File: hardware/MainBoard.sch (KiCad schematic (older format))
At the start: 33 parts, among them P1 CONN_01X07, P2 CONN_01X04, P3 CONN_01X04, P4 CONN_01X07, P5 ON/OFF, P6 BATTERY

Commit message: Fix schematic libraries
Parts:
- P?: symbol USB_OTG -> USB_OTG-RESCUE-MainBoard
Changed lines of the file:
@@
 EESchema Schematic File Version 2
+LIBS:MainBoard-rescue
 LIBS:power
 LIBS:device
@@
 LIBS:contrib
 LIBS:valves
-LIBS:ATSAMD21G18A-AU
-LIBS:MCP73831T-2ACI_OT
-LIBS:theinventorhouse
-LIBS:B3U-1000P
 LIBS:MainBoard-cache
 EELAYER 25 0
@@
 $Bitmap
 Pos 9695 7065
-Scale 1,000000
+Scale 1.000000
 Data
 89 50 4E 47 0D 0A 1A 0A 00 00 00 0D 49 48 44 52 00 00 01 77 00 00 01 29 08 06 00 00 00 68 44 62
@@
 POWER, CHARGER & FILTERING
 $Comp
-L USB_OTG P?
+L USB_OTG-RESCUE-MainBoard P?
 U 1 1 5AD40F68
 P 8980 975

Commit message: check button
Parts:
- removed S?: B3U-1000P, SW_B3U-1000P, symbol B3U-1000P
- added R?: 10k, symbol R_Small
- added SW?: SW_Push, symbol SW_Push
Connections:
- net +3V3: now also R?.2
- net GND: now also SW?.1
- net RESET: now also R?.1, SW?.2
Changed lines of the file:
@@
 EESchema Schematic File Version 2
-LIBS:MainBoard-rescue
 LIBS:power
 LIBS:device
@@
 LIBS:contrib
 LIBS:valves
+LIBS:CatSatZero
+LIBS:74xgxx
+LIBS:ac-dc
+LIBS:actel
+LIBS:allegro
+LIBS:Altera
+LIBS:analog_devices
+LIBS:battery_management
+LIBS:bbd
+LIBS:bosch
+LIBS:brooktre
+LIBS:cmos_ieee
+LIBS:dc-dc
+LIBS:diode
+LIBS:elec-unifil
+LIBS:ESD_Protection
+LIBS:ftdi
+LIBS:gennum
+LIBS:graphic_symbols
+LIBS:hc11
+LIBS:infineon
+LIBS:intersil
+LIBS:ir
+LIBS:Lattice
+LIBS:leds
+LIBS:LEM
+LIBS:logic_programmable
+LIBS:maxim
+LIBS:mechanical
+LIBS:microchip_dspic33dsc
+LIBS:microchip_pic10mcu
+LIBS:microchip_pic12mcu
+LIBS:microchip_pic16mcu
+LIBS:microchip_pic18mcu
+LIBS:microchip_pic24mcu
+LIBS:microchip_pic32mcu
+LIBS:modules
+LIBS:motor_drivers
+LIBS:motors
+LIBS:msp430
+LIBS:nordicsemi
+LIBS:nxp_armmcu
+LIBS:nxp
+LIBS:onsemi
+LIBS:Oscillators
+LIBS:Power_Management
+LIBS:powerint
+LIBS:pspice
+LIBS:references
+LIBS:relays
+LIBS:rfcom
+LIBS:RFSolutions
+LIBS:sensors
+LIBS:silabs
+LIBS:stm8
+LIBS:stm32
+LIBS:supertex
+LIBS:switches
+LIBS:transf
+LIBS:triac_thyristor
+LIBS:ttl_ieee
+LIBS:video
+LIBS:wiznet
+LIBS:Worldsemi
+LIBS:Xicor
+LIBS:zetex
+LIBS:Zilog
 LIBS:MainBoard-cache
 EELAYER 25 0
@@
 	1    0    0    -1
 $EndComp
-$Comp
-L B3U-1000P S?
-U 1 1 5AD4D846
-P 6510 4980
-F 0 "S?" H 6209 5181 50  0000 L BNN
-F 1 "B3U-1000P" H 6209 4679 50  0000 L BNN
-F 2 "SW_B3U-1000P" H 6510 4980 50  0001 L BNN
-F 3 "None" H 6510 4980 50  0001 L BNN
-F 4 "Omron" H 6510 4980 50  0001 L BNN "Campo4"
-F 5 "B3U-1000P" H 6510 4980 50  0001 L BNN "Campo5"
-F 6 "Switch Tactile N.O. SPST Round Button Gull Wing 0.05A 12VDC 1.5N SMD Embossed T/R" H 6510 4980 50  0001 L BNN "Campo6"
-F 7 "0.69 USD" H 6510 4980 50  0001 L BNN "Campo7"
-F 8 "Good" H 6510 4980 50  0001 L BNN "Campo8"
-	1    6510 4980
-	1    0    0    -1
-$EndComp
-Text Label 7155 4980 0    60   ~ 0
+Text Label 6655 5145 0    60   ~ 0
 RESET
 $Comp
 L GND #PWR?
 U 1 1 5AD4E61D
-P 5875 5030
-F 0 "#PWR?" H 5875 4780 50  0001 C CNN
-F 1 "GND" H 5875 4880 50  0000 C CNN
-F 2 "" H 5875 5030 50  0000 C CNN
-F 3 "" H 5875 5030 50  0000 C CNN
-	1    5875 5030
+P 5725 5195
+F 0 "#PWR?" H 5725 4945 50  0001 C CNN
+F 1 "GND" H 5725 5045 50  0000 C CNN
+F 2 "" H 5725 5195 50  0000 C CNN
+F 3 "" H 5725 5195 50  0000 C CNN
+	1    5725 5195
 	1    0    0    -1
 $EndComp
@@
 	3555 2405 3700 2405
 Wire Wire Line
-	3700 2405 3700 1925
+	3700 2405 3700 2305
+Wire Wire Line
+	3700 2305 3700 2205
+Wire Wire Line
+	3700 2205 3700 2105
+Wire Wire Line
+	3700 2105 3700 1925
 Wire Wire Line
 	3555 2305 3700 2305
@@
 	3555 4805 3605 4805
 Wire Wire Line
-	3605 4805 3605 5185
+	3605 4805 3605 4905
+Wire Wire Line
+	3605 4905 3605 5005
+Wire Wire Line
+	3605 5005 3605 5105
+Wire Wire Line
+	3605 5105 3605 5185
 Wire Wire Line
 	3555 5105 3605 5105
@@
 	11205 3355 11205 3365
 Wire Wire Line
-	8650 2595 9520 2595
+	8650 2595 8895 2595
+Wire Wire Line
+	8895 2595 9110 2595
+Wire Wire Line
+	9110 2595 9520 2595
 Wire Wire Line
 	8895 2595 8895 2465
@@
 Connection ~ 8895 2595
 Wire Wire Line
-	10470 2595 10985 2595
+	10470 2595 10520 2595
+Wire Wire Line
+	10520 2595 10710 2595
+Wire Wire Line
+	10710 2595 10885 2595
+Wire Wire Line
+	10885 2595 10985 2595
 Wire Wire Line
 	10885 2595 10885 2640
@@
 	10520 2840 10520 2945
 Wire Wire Line
-	10710 2840 10710 3005
+	10710 2840 10710 2945
+Wire Wire Line
+	10710 2945 10710 3005
 Wire Wire Line
 	10885 2945 10885 2840
 Wire Wire Line
-	10520 2945 10885 2945
+	10520 2945 10710 2945
+Wire Wire Line
+	10710 2945 10885 2945
 Connection ~ 10710 2945
 Wire Notes Line
@@
 	5275 6540 6965 6540
 Wire Wire Line
-	5450 2500 5450 2585
+	5450 2500 5450 2540
+Wire Wire Line
+	5450 2540 5450 2585
 Wire Wire Line
 	5450 2785 5450 2845
@@
 	6060 2225 6060 2080
 Wire Wire Line
-	6010 4980 5875 4980
-Wire Wire Line
-	5875 4980 5875 5030
-Wire Wire Line
-	7010 4980 7155 4980
+	5860 5145 5725 5145
+Wire Wire Line
+	5725 5145 5725 5195
+Wire Wire Line
+	6260 5145 6505 5145
+Wire Wire Line
+	6505 5145 6655 5145
 Wire Wire Line
 	2155 3905 1990 3905
@@
 	8135 4285 8135 4315
 Wire Wire Line
-	1435 1940 1435 2405
-Wire Wire Line
-	1235 1940 1235 2505
+	1435 1940 1435 2100
+Wire Wire Line
+	1435 2100 1435 2405
+Wire Wire Line
+	1235 1940 1235 2100
+Wire Wire Line
+	1235 2100 1235 2505
 Connection ~ 1435 2100
 Connection ~ 1235 2100
@@
 	1345 1550 1345 1630
 Wire Wire Line
-	1235 1630 1435 1630
+	1235 1630 1345 1630
+Wire Wire Line
+	1345 1630 1435 1630
 Connection ~ 1345 1630
 Wire Wire Line
@@
 	1    0    0    -1
 $EndComp
+$Comp
+L +3.3V #PWR?
+U 1 1 5AD55919
+P 6505 4730
+F 0 "#PWR?" H 6505 4580 50  0001 C CNN
+F 1 "+3.3V" H 6505 4870 50  0000 C CNN
+F 2 "" H 6505 4730 50  0000 C CNN
+F 3 "" H 6505 4730 50  0000 C CNN
+	1    6505 4730
+	1    0    0    -1
+$EndComp
+$Comp
+L R_Small R?
+U 1 1 5AD55C99
+P 6505 4905
+F 0 "R?" H 6535 4925 50  0000 L CNN
+F 1 "10k" H 6535 4865 50  0000 L CNN
+F 2 "" H 6505 4905 50  0000 C CNN
+F 3 "" H 6505 4905 50  0000 C CNN
+	1    6505 4905
+	-1   0    0    1
+$EndComp
+Wire Wire Line
+	6505 4730 6505 4805
+Wire Wire Line
+	6505 5005 6505 5145
+Connection ~ 6505 5145
+$Comp
+L SW_Push SW?
+U 1 1 5AD574E0
+P 6060 5145
+F 0 "SW?" H 6110 5245 50  0000 L CNN
+F 1 "SW_Push" H 6060 5085 50  0000 C CNN
+F 2 "" H 6060 5345 50  0001 C CNN
+F 3 "" H 6060 5345 50  0001 C CNN
+	1    6060 5145
+	1    0    0    -1
+$EndComp

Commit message: Shottcky diode fix
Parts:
- removed D?: MBR120, symbol D_Schottky
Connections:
- net VCC: now also C?.1, D?.1 (K), U?.3 (IN)
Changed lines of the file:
@@
-$EndComp
-$Comp
-L D_Schottky D?
-U 1 1 5AD43E7A
-P 8650 2315
-F 0 "D?" H 8650 2415 50  0000 C CNN
-F 1 "MBR120" H 8645 2245 50  0000 C CNN
-F 2 "" H 8650 2315 50  0000 C CNN
-F 3 "" H 8650 2315 50  0000 C CNN
-	1    8650 2315
-	0    -1   -1   0
 $EndComp
 $Comp
@@
 	2155 2605 1970 2605
 Wire Wire Line
-	3555 2405 3700 2405
-Wire Wire Line
-	3700 2405 3700 2305
-Wire Wire Line
-	3700 2305 3700 2205
-Wire Wire Line
-	3700 2205 3700 2105
-Wire Wire Line
-	3700 2105 3700 1925
+	3700 2405 3555 2405
+Wire Wire Line
+	3700 1925 3700 2405
 Wire Wire Line
 	3555 2305 3700 2305
@@
 	3555 4805 3605 4805
 Wire Wire Line
-	3605 4805 3605 4905
-Wire Wire Line
-	3605 4905 3605 5005
-Wire Wire Line
-	3605 5005 3605 5105
-Wire Wire Line
-	3605 5105 3605 5185
+	3605 4805 3605 5185
 Wire Wire Line
 	3555 5105 3605 5105
@@
 	11205 3355 11205 3365
 Wire Wire Line
-	8650 2595 8895 2595
-Wire Wire Line
-	8895 2595 9110 2595
-Wire Wire Line
-	9110 2595 9520 2595
+	8650 2595 9520 2595
 Wire Wire Line
 	8895 2595 8895 2465
@@
 	8895 2165 8895 2085
 Wire Wire Line
-	8650 2595 8650 2465
+	8650 2100 8650 2595
 Connection ~ 8895 2595
 Wire Wire Line
-	10470 2595 10520 2595
-Wire Wire Line
-	10520 2595 10710 2595
-Wire Wire Line
-	10710 2595 10885 2595
-Wire Wire Line
-	10885 2595 10985 2595
+	10470 2595 10985 2595
 Wire Wire Line
 	10885 2595 10885 2640
@@
 	10520 2840 10520 2945
 Wire Wire Line
-	10710 2840 10710 2945
-Wire Wire Line
-	10710 2945 10710 3005
+	10710 2840 10710 3005
 Wire Wire Line
 	10885 2945 10885 2840
 Wire Wire Line
-	10520 2945 10710 2945
-Wire Wire Line
-	10710 2945 10885 2945
+	10520 2945 10885 2945
 Connection ~ 10710 2945
 Wire Notes Line
@@
 	8290 2225 8290 2130
 Wire Wire Line
-	8650 2165 8650 2100
-Wire Wire Line
 	8330 680  8330 775
 Wire Wire Line
@@
 	5275 6540 6965 6540
 Wire Wire Line
-	5450 2500 5450 2540
-Wire Wire Line
-	5450 2540 5450 2585
+	5450 2500 5450 2585
 Wire Wire Line
 	5450 2785 5450 2845
@@
 	5725 5145 5725 5195
 Wire Wire Line
-	6260 5145 6505 5145
-Wire Wire Line
-	6505 5145 6655 5145
+	6260 5145 6655 5145
 Wire Wire Line
 	2155 3905 1990 3905
@@
 	8135 4285 8135 4315
 Wire Wire Line
-	1435 1940 1435 2100
-Wire Wire Line
-	1435 2100 1435 2405
-Wire Wire Line
-	1235 1940 1235 2100
-Wire Wire Line
-	1235 2100 1235 2505
+	1435 1940 1435 2405
+Wire Wire Line
+	1235 1940 1235 2505
 Connection ~ 1435 2100
 Connection ~ 1235 2100
@@
 	1345 1550 1345 1630
 Wire Wire Line
-	1235 1630 1345 1630
-Wire Wire Line
-	1345 1630 1435 1630
+	1235 1630 1435 1630
 Connection ~ 1345 1630
 Wire Wire Line

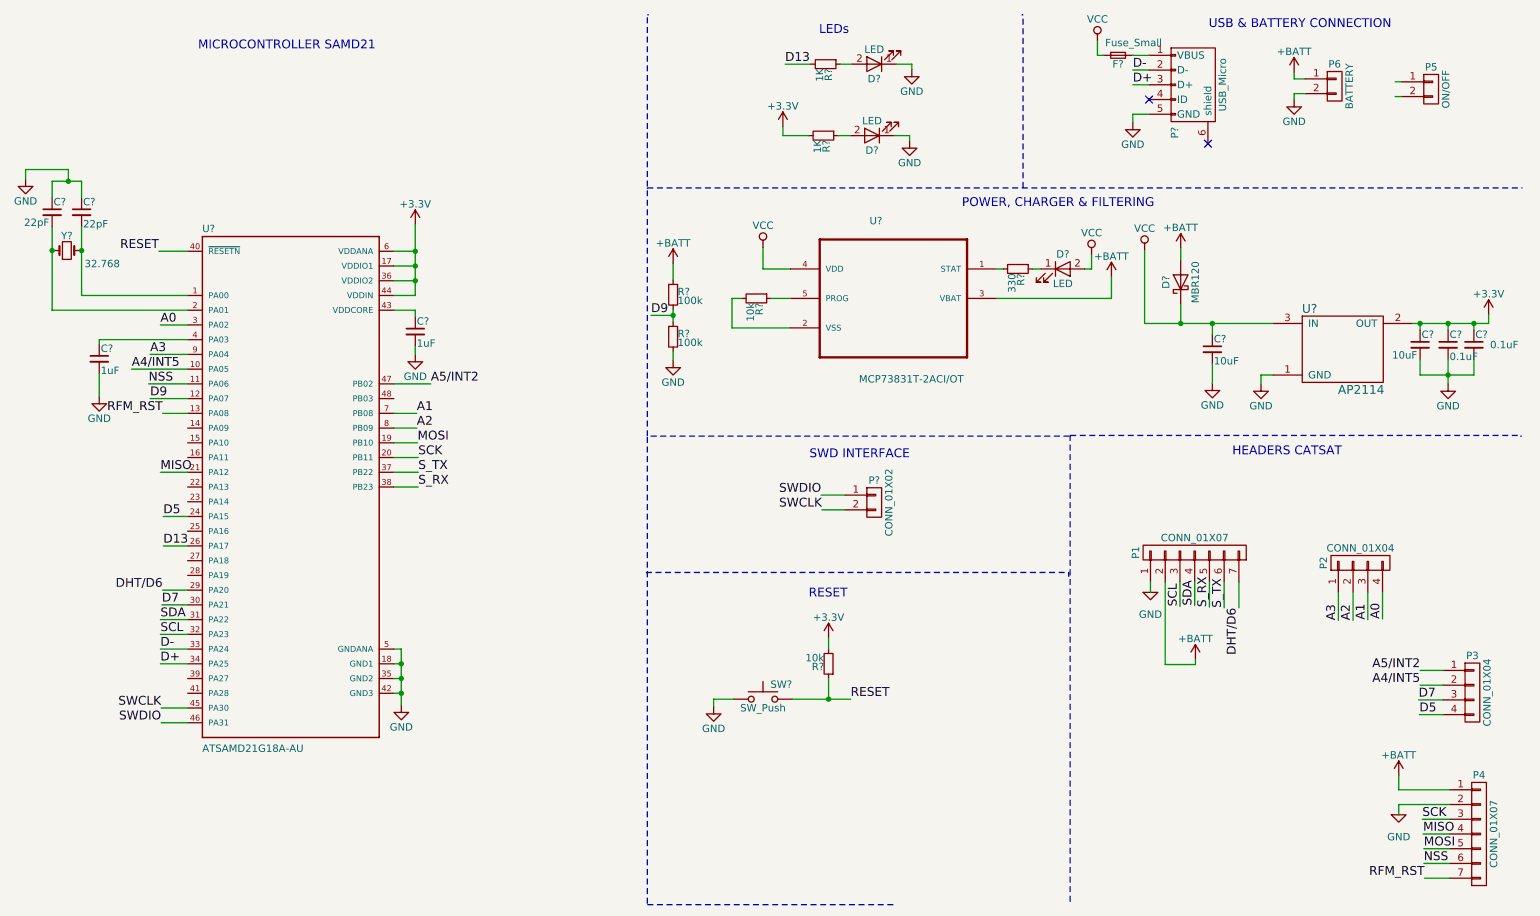
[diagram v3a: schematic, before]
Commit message: Assign footprints
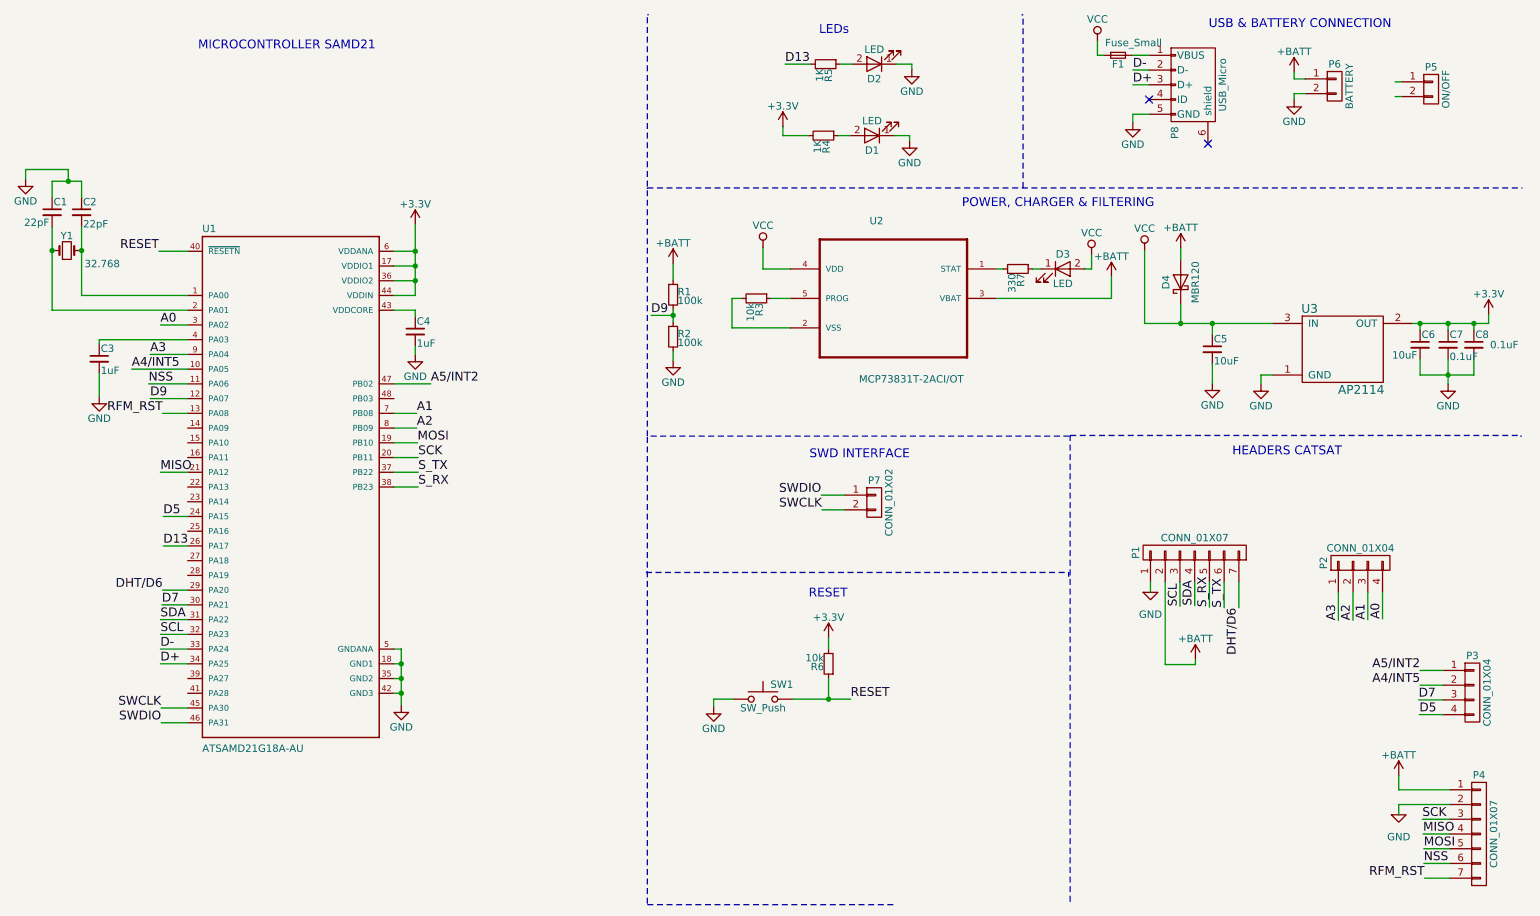
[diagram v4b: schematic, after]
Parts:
- C1, C2, C3, C4, C5, C6, C7, C8: renamed from C?; footprint (none) -> Capacitors_SMD:C_0805_HandSoldering
- D1, D2, D3: renamed from D?; footprint (none) -> LEDs:LED_0805_HandSoldering
- P8: renamed from P?; footprint (none) -> Connect:USB_Micro-B_10103594-0001LF
- R1, R2, R3, R4, R5, R6, R7: renamed from R?; footprint (none) -> Resistors_SMD:R_0805_HandSoldering
- SW1: renamed from SW?; footprint (none) -> TIH:SW_B3U-1000P
- U1: renamed from U?; footprint QFP50P900X900X120-48N -> Housings_QFP:TQFP-48_7x7mm_Pitch0.5mm
- U2: renamed from U?; footprint SOT95P280X145-5N -> TO_SOT_Packages_SMD:SOT-23-5
- U3: renamed from U?; footprint (none) -> TO_SOT_Packages_SMD:SOT-223-3_TabPin2
- gave numbers to parts that had none: 4

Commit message: Update netlist
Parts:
- D4: footprint (none) -> Diodes_SMD:D_SOD-123F
- P7: footprint (none) -> Pin_Headers:Pin_Header_Straight_1x02_Pitch2.54mm
- Y1: footprint (none) -> TIH:LFXTAL016178Reel
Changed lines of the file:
@@
 F 0 "D4" H 8895 2415 50  0000 C CNN
 F 1 "MBR120" H 8895 2215 50  0000 C CNN
-F 2 "" H 8895 2315 50  0001 C CNN
+F 2 "Diodes_SMD:D_SOD-123F" H 8895 2315 50  0001 C CNN
 F 3 "" H 8895 2315 50  0000 C CNN
 	1    8895 2315
@@
 F 0 "P7" H 6815 3960 50  0000 C CNN
 F 1 "CONN_01X02" V 6915 3810 50  0000 C CNN
-F 2 "" H 6815 3810 50  0001 C CNN
+F 2 "Pin_Headers:Pin_Header_Straight_1x02_Pitch2.54mm" H 6815 3810 50  0001 C CNN
 F 3 "" H 6815 3810 50  0000 C CNN
 	1    6815 3810
@@
 F 0 "Y1" H 1335 2200 50  0000 C CNN
 F 1 "32.768" H 1575 2010 50  0000 C CNN
-F 2 "" H 1335 2100 50  0001 C CNN
+F 2 "TIH:LFXTAL016178Reel" H 1335 2100 50  0001 C CNN
 F 3 "" H 1335 2100 50  0000 C CNN
 	1    1335 2100

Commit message: Update for MakeCode
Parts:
- removed C1, C2: 22pF, Capacitors_SMD:C_0805_HandSoldering, symbol C_Small
- removed P7: CONN_01X02, Pin_Headers:Pin_Header_Straight_1x02_Pitch2.54mm, symbol CONN_01X02
- removed R6: 10k, Resistors_SMD:R_0805_HandSoldering, symbol R_Small
- removed Y1: 32.768, TIH:LFXTAL016178Reel, symbol Crystal_Small
- added P7: CONN_01X04, Pines:61300411121, symbol conn:CONN_01X04
- C3, C4, C5, C6, C7, C8: symbol C_Small -> device:C_Small
- D1, D2, D3: symbol LED -> device:LED
- D4: symbol D_Schottky -> device:D_Schottky
- F1: symbol Fuse_Small -> device:Fuse_Small
- P1, P4: symbol CONN_01X07 -> conn:CONN_01X07
- P2, P3: symbol CONN_01X04 -> conn:CONN_01X04
- P5, P6: symbol CONN_01X02 -> conn:CONN_01X02
- P8: symbol USB_OTG-RESCUE-MainBoard -> CatSatZero:USB_OTG-RESCUE-MainBoard
- R1, R2, R3, R4, R5, R7: symbol R_Small -> device:R_Small
- SW1: value SW_Push -> RESET; symbol SW_Push -> CatSatZero:SW_Push
- U1: symbol ATSAMD21G18A-AU -> CatSatZero:ATSAMD21G18A-AU
- U2: symbol MCP73831T-2ACI/OT -> MainBoard-rescue:MCP73831T-2ACI_OT
- U3: symbol AP2114 -> CatSatZero:AP2114
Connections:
- net labels added: +3V3, 3.3v, A5
- net labels removed: D9
- wire segments 139 -> 143
- no-connect marks 2 -> 15
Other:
- moved on the sheet: F1, P5, P6, P8, R1, R2
